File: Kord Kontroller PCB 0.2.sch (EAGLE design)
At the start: 190 parts, among them J1 MIDIOUTB, J2 MIDIOUTA, J3 FTSH-105-01-L-DV-KJ, SW2 SPST_TACT-KMR2, U1 AP2112K-3.3, U2 ATSAMD51J19A-AUT, U3 SN74LV4T125PWR, Y1 ECS-.327-12.5-17X-TR

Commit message: LED Variant and rewire
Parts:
- LED1, LED10, LED11, LED12, LED13, LED14, LED15, LED16, LED17, LED18, LED19, LED2, LED20, LED21, LED22, LED23, LED24, LED25, LED26, LED27, LED28, LED29, LED3, LED30, LED31, LED32, LED33, LED34, LED35, LED36, LED37, LED38, LED39, LED4, LED40, LED41, LED42, LED43, LED44, LED45, LED46, LED47, LED48, LED49, LED5, LED50, LED51, LED52, LED53, LED54, LED6, LED7, LED8, LED9: value WS2812B3535 -> WS2812BHRGB32M; device microbuilder:WS2812B3535 -> adafruit:WS2812BHRGB32M
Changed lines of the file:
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@@
 <part name="B10" library="microbuilder" deviceset="ELAST_10X10" device=""/>
 <part name="B14" library="microbuilder" deviceset="ELAST_10X10" device=""/>
-<part name="LED1" library="microbuilder" deviceset="WS2812B" device="3535"/>
-<part name="LED2" library="microbuilder" deviceset="WS2812B" device="3535"/>
-<part name="LED3" library="microbuilder" deviceset="WS2812B" device="3535"/>
-<part name="LED4" library="microbuilder" deviceset="WS2812B" device="3535"/>
-<part name="LED5" library="microbuilder" deviceset="WS2812B" device="3535"/>
-<part name="LED6" library="microbuilder" deviceset="WS2812B" device="3535"/>
-<part name="LED7" library="microbuilder" deviceset="WS2812B" device="3535"/>
-<part name="LED8" library="microbuilder" deviceset="WS2812B" device="3535"/>
-<part name="LED9" library="microbuilder" deviceset="WS2812B" device="3535"/>
-<part name="LED10" library="microbuilder" deviceset="WS2812B" device="3535"/>
-<part name="LED11" library="microbuilder" deviceset="WS2812B" device="3535"/>
-<part name="LED12" library="microbuilder" deviceset="WS2812B" device="3535"/>
-<part name="LED13" library="microbuilder" deviceset="WS2812B" device="3535"/>
-<part name="LED14" library="microbuilder" deviceset="WS2812B" device="3535"/>
-<part name="LED15" library="microbuilder" deviceset="WS2812B" device="3535"/>
-<part name="LED16" library="microbuilder" deviceset="WS2812B" device="3535"/>
+<part name="LED1" library="adafruit" deviceset="WS2812B" device="HRGB32M"/>
+<part name="LED2" library="adafruit" deviceset="WS2812B" device="HRGB32M"/>
+<part name="LED3" library="adafruit" deviceset="WS2812B" device="HRGB32M"/>
+<part name="LED4" library="adafruit" deviceset="WS2812B" device="HRGB32M"/>
+<part name="LED5" library="adafruit" deviceset="WS2812B" device="HRGB32M"/>
+<part name="LED6" library="adafruit" deviceset="WS2812B" device="HRGB32M"/>
+<part name="LED7" library="adafruit" deviceset="WS2812B" device="HRGB32M"/>
+<part name="LED8" library="adafruit" deviceset="WS2812B" device="HRGB32M"/>
+<part name="LED9" library="adafruit" deviceset="WS2812B" device="HRGB32M"/>
+<part name="LED10" library="adafruit" deviceset="WS2812B" device="HRGB32M"/>
+<part name="LED11" library="adafruit" deviceset="WS2812B" device="HRGB32M"/>
+<part name="LED12" library="adafruit" deviceset="WS2812B" device="HRGB32M"/>
+<part name="LED13" library="adafruit" deviceset="WS2812B" device="HRGB32M"/>
+<part name="LED14" library="adafruit" deviceset="WS2812B" device="HRGB32M"/>
+<part name="LED15" library="adafruit" deviceset="WS2812B" device="HRGB32M"/>
+<part name="LED16" library="adafruit" deviceset="WS2812B" device="HRGB32M"/>
 <part name="GND1" library="supply1" library_urn="urn:adsk.eagle:library:371" deviceset="GND" device=""/>
 <part name="GND8" library="supply1" library_urn="urn:adsk.eagle:library:371" deviceset="GND" device=""/>
-<part name="LED17" library="microbuilder" deviceset="WS2812B" device="3535"/>
-<part name="LED18" library="microbuilder" deviceset="WS2812B" device="3535"/>
-<part name="LED19" library="microbuilder" deviceset="WS2812B" device="3535"/>
-<part name="LED20" library="microbuilder" deviceset="WS2812B" device="3535"/>
-<part name="LED21" library="microbuilder" deviceset="WS2812B" device="3535"/>
-<part name="LED22" library="microbuilder" deviceset="WS2812B" device="3535"/>
-<part name="LED23" library="microbuilder" deviceset="WS2812B" device="3535"/>
-<part name="LED24" library="microbuilder" deviceset="WS2812B" device="3535"/>
-<part name="LED25" library="microbuilder" deviceset="WS2812B" device="3535"/>
-<part name="LED26" library="microbuilder" deviceset="WS2812B" device="3535"/>
-<part name="LED27" library="microbuilder" deviceset="WS2812B" device="3535"/>
-<part name="LED28" library="microbuilder" deviceset="WS2812B" device="3535"/>
-<part name="LED29" library="microbuilder" deviceset="WS2812B" device="3535"/>
-<part name="LED30" library="microbuilder" deviceset="WS2812B" device="3535"/>
-<part name="LED31" library="microbuilder" deviceset="WS2812B" device="3535"/>
-<part name="LED32" library="microbuilder" deviceset="WS2812B" device="3535"/>
+<part name="LED17" library="adafruit" deviceset="WS2812B" device="HRGB32M"/>
+<part name="LED18" library="adafruit" deviceset="WS2812B" device="HRGB32M"/>
+<part name="LED19" library="adafruit" deviceset="WS2812B" device="HRGB32M"/>
+<part name="LED20" library="adafruit" deviceset="WS2812B" device="HRGB32M"/>
+<part name="LED21" library="adafruit" deviceset="WS2812B" device="HRGB32M"/>
+<part name="LED22" library="adafruit" deviceset="WS2812B" device="HRGB32M"/>
+<part name="LED23" library="adafruit" deviceset="WS2812B" device="HRGB32M"/>
+<part name="LED24" library="adafruit" deviceset="WS2812B" device="HRGB32M"/>
+<part name="LED25" library="adafruit" deviceset="WS2812B" device="HRGB32M"/>
+<part name="LED26" library="adafruit" deviceset="WS2812B" device="HRGB32M"/>
+<part name="LED27" library="adafruit" deviceset="WS2812B" device="HRGB32M"/>
+<part name="LED28" library="adafruit" deviceset="WS2812B" device="HRGB32M"/>
+<part name="LED29" library="adafruit" deviceset="WS2812B" device="HRGB32M"/>
+<part name="LED30" library="adafruit" deviceset="WS2812B" device="HRGB32M"/>
+<part name="LED31" library="adafruit" deviceset="WS2812B" device="HRGB32M"/>
+<part name="LED32" library="adafruit" deviceset="WS2812B" device="HRGB32M"/>
 <part name="GND11" library="supply1" library_urn="urn:adsk.eagle:library:371" deviceset="GND" device=""/>
 <part name="GND12" library="supply1" library_urn="urn:adsk.eagle:library:371" deviceset="GND" device=""/>
@@
 <part name="U$13" library="microbuilder" deviceset="3.3V" device=""/>
 <part name="PTC1" library="microbuilder" deviceset="PTC" device="1206" value="500mA Fuse"/>
-<part name="LED33" library="microbuilder" deviceset="WS2812B" device="3535"/>
-<part name="LED34" library="microbuilder" deviceset="WS2812B" device="3535"/>
-<part name="LED35" library="microbuilder" deviceset="WS2812B" device="3535"/>
-<part name="LED36" library="microbuilder" deviceset="WS2812B" device="3535"/>
-<part name="LED37" library="microbuilder" deviceset="WS2812B" device="3535"/>
-<part name="LED38" library="microbuilder" deviceset="WS2812B" device="3535"/>
-<part name="LED39" library="microbuilder" deviceset="WS2812B" device="3535"/>
-<part name="LED40" library="microbuilder" deviceset="WS2812B" device="3535"/>
+<part name="LED33" library="adafruit" deviceset="WS2812B" device="HRGB32M"/>
+<part name="LED34" library="adafruit" deviceset="WS2812B" device="HRGB32M"/>
+<part name="LED35" library="adafruit" deviceset="WS2812B" device="HRGB32M"/>
+<part name="LED36" library="adafruit" deviceset="WS2812B" device="HRGB32M"/>
+<part name="LED37" library="adafruit" deviceset="WS2812B" device="HRGB32M"/>
+<part name="LED38" library="adafruit" deviceset="WS2812B" device="HRGB32M"/>
+<part name="LED39" library="adafruit" deviceset="WS2812B" device="HRGB32M"/>
+<part name="LED40" library="adafruit" deviceset="WS2812B" device="HRGB32M"/>
 <part name="GND10" library="supply1" library_urn="urn:adsk.eagle:library:371" deviceset="GND" device=""/>
-<part name="LED41" library="microbuilder" deviceset="WS2812B" device="3535"/>
-<part name="LED42" library="microbuilder" deviceset="WS2812B" device="3535"/>
-<part name="LED43" library="microbuilder" deviceset="WS2812B" device="3535"/>
-<part name="LED44" library="microbuilder" deviceset="WS2812B" device="3535"/>
-<part name="LED45" library="microbuilder" deviceset="WS2812B" device="3535"/>
-<part name="LED46" library="microbuilder" deviceset="WS2812B" device="3535"/>
-<part name="LED47" library="microbuilder" deviceset="WS2812B" device="3535"/>
-<part name="LED48" library="microbuilder" deviceset="WS2812B" device="3535"/>
+<part name="LED41" library="adafruit" deviceset="WS2812B" device="HRGB32M"/>
+<part name="LED42" library="adafruit" deviceset="WS2812B" device="HRGB32M"/>
+<part name="LED43" library="adafruit" deviceset="WS2812B" device="HRGB32M"/>
+<part name="LED44" library="adafruit" deviceset="WS2812B" device="HRGB32M"/>
+<part name="LED45" library="adafruit" deviceset="WS2812B" device="HRGB32M"/>
+<part name="LED46" library="adafruit" deviceset="WS2812B" device="HRGB32M"/>
+<part name="LED47" library="adafruit" deviceset="WS2812B" device="HRGB32M"/>
+<part name="LED48" library="adafruit" deviceset="WS2812B" device="HRGB32M"/>
 <part name="GND16" library="supply1" library_urn="urn:adsk.eagle:library:371" deviceset="GND" device=""/>
-<part name="LED49" library="microbuilder" deviceset="WS2812B" device="3535"/>
-<part name="LED50" library="microbuilder" deviceset="WS2812B" device="3535"/>
-<part name="LED51" library="microbuilder" deviceset="WS2812B" device="3535"/>
-<part name="LED52" library="microbuilder" deviceset="WS2812B" device="3535"/>
-<part name="LED53" library="microbuilder" deviceset="WS2812B" device="3535"/>
-<part name="LED54" library="microbuilder" deviceset="WS2812B" device="3535"/>
+<part name="LED49" library="adafruit" deviceset="WS2812B" device="HRGB32M"/>
+<part name="LED50" library="adafruit" deviceset="WS2812B" device="HRGB32M"/>
+<part name="LED51" library="adafruit" deviceset="WS2812B" device="HRGB32M"/>
+<part name="LED52" library="adafruit" deviceset="WS2812B" device="HRGB32M"/>
+<part name="LED53" library="adafruit" deviceset="WS2812B" device="HRGB32M"/>
+<part name="LED54" library="adafruit" deviceset="WS2812B" device="HRGB32M"/>
 <part name="GND17" library="supply1" library_urn="urn:adsk.eagle:library:371" deviceset="GND" device=""/>
 <part name="R3" library="SparkFun-Resistors" deviceset="220OHM-1/10W-1%(0603)" device="" value="220"/>

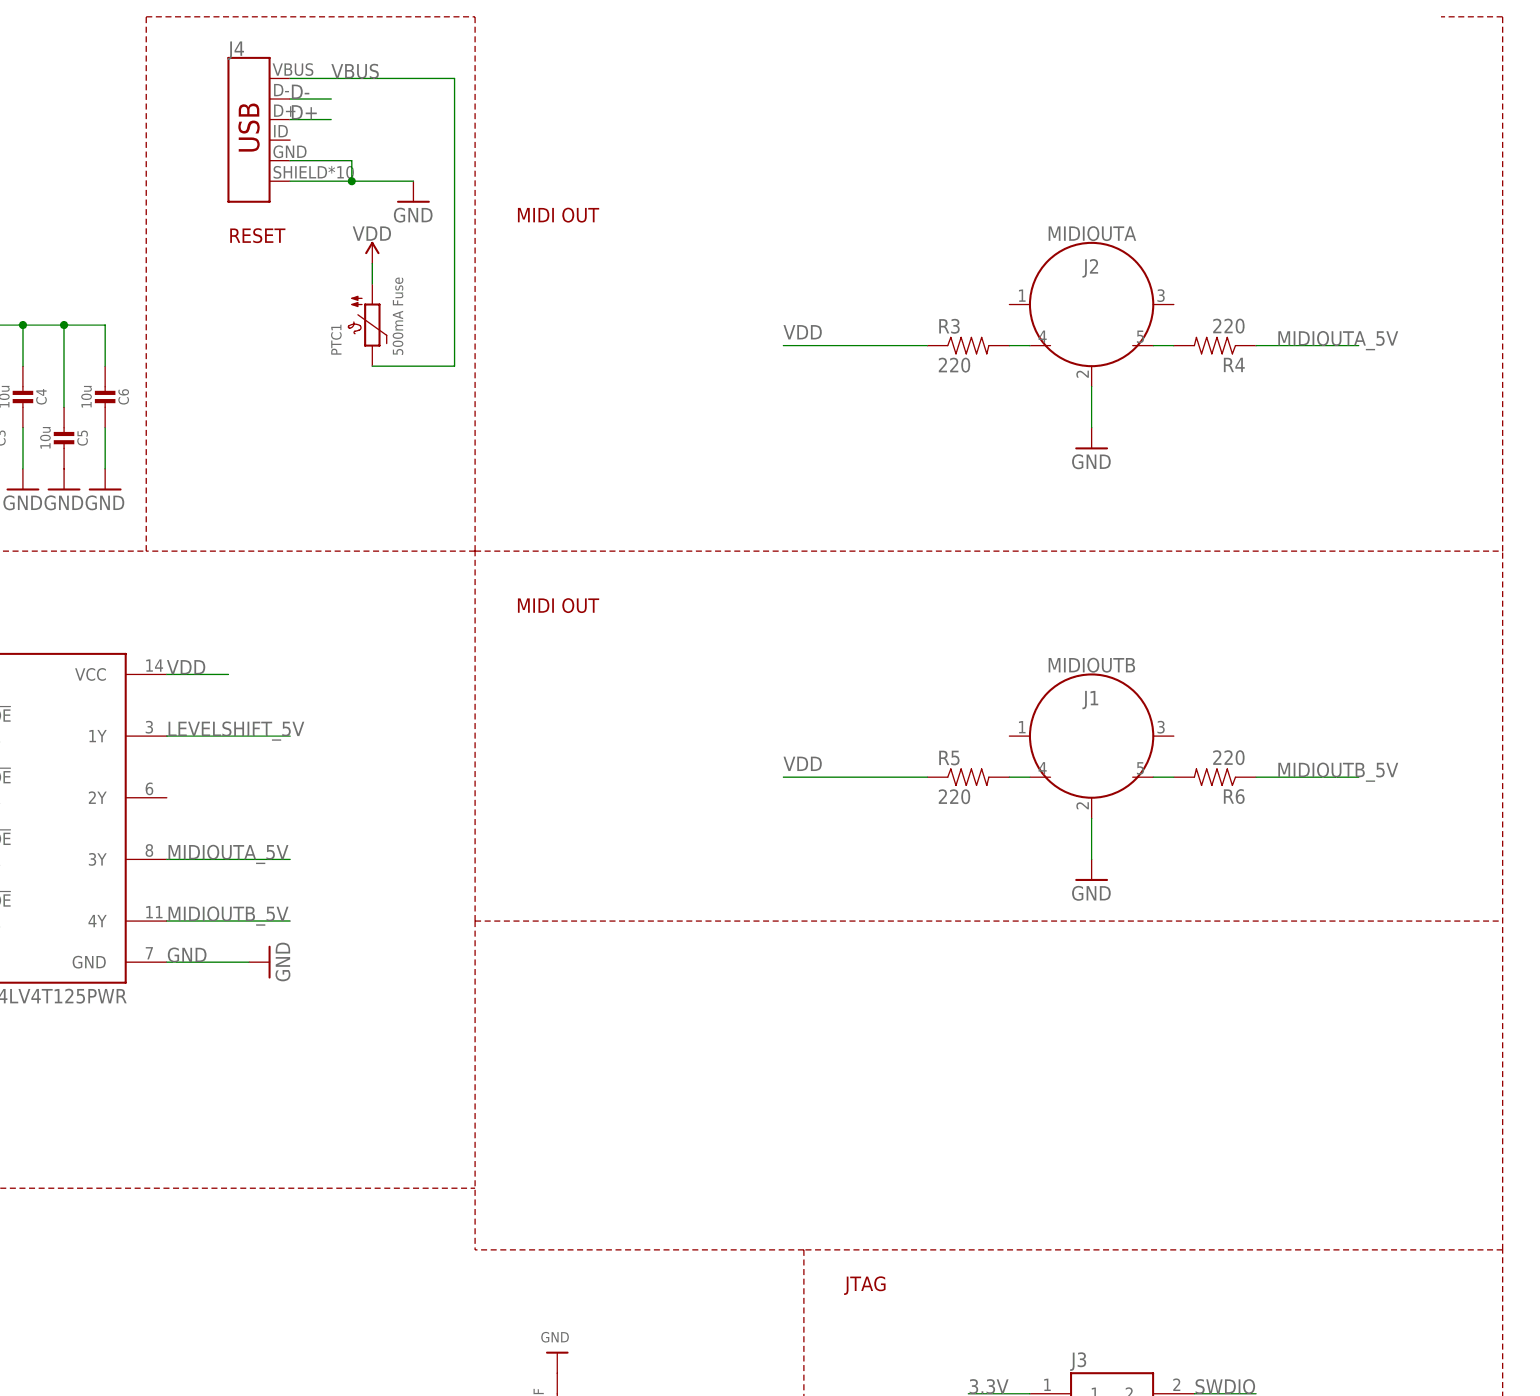
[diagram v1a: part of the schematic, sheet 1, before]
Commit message: added 2.5 mmtrs parts
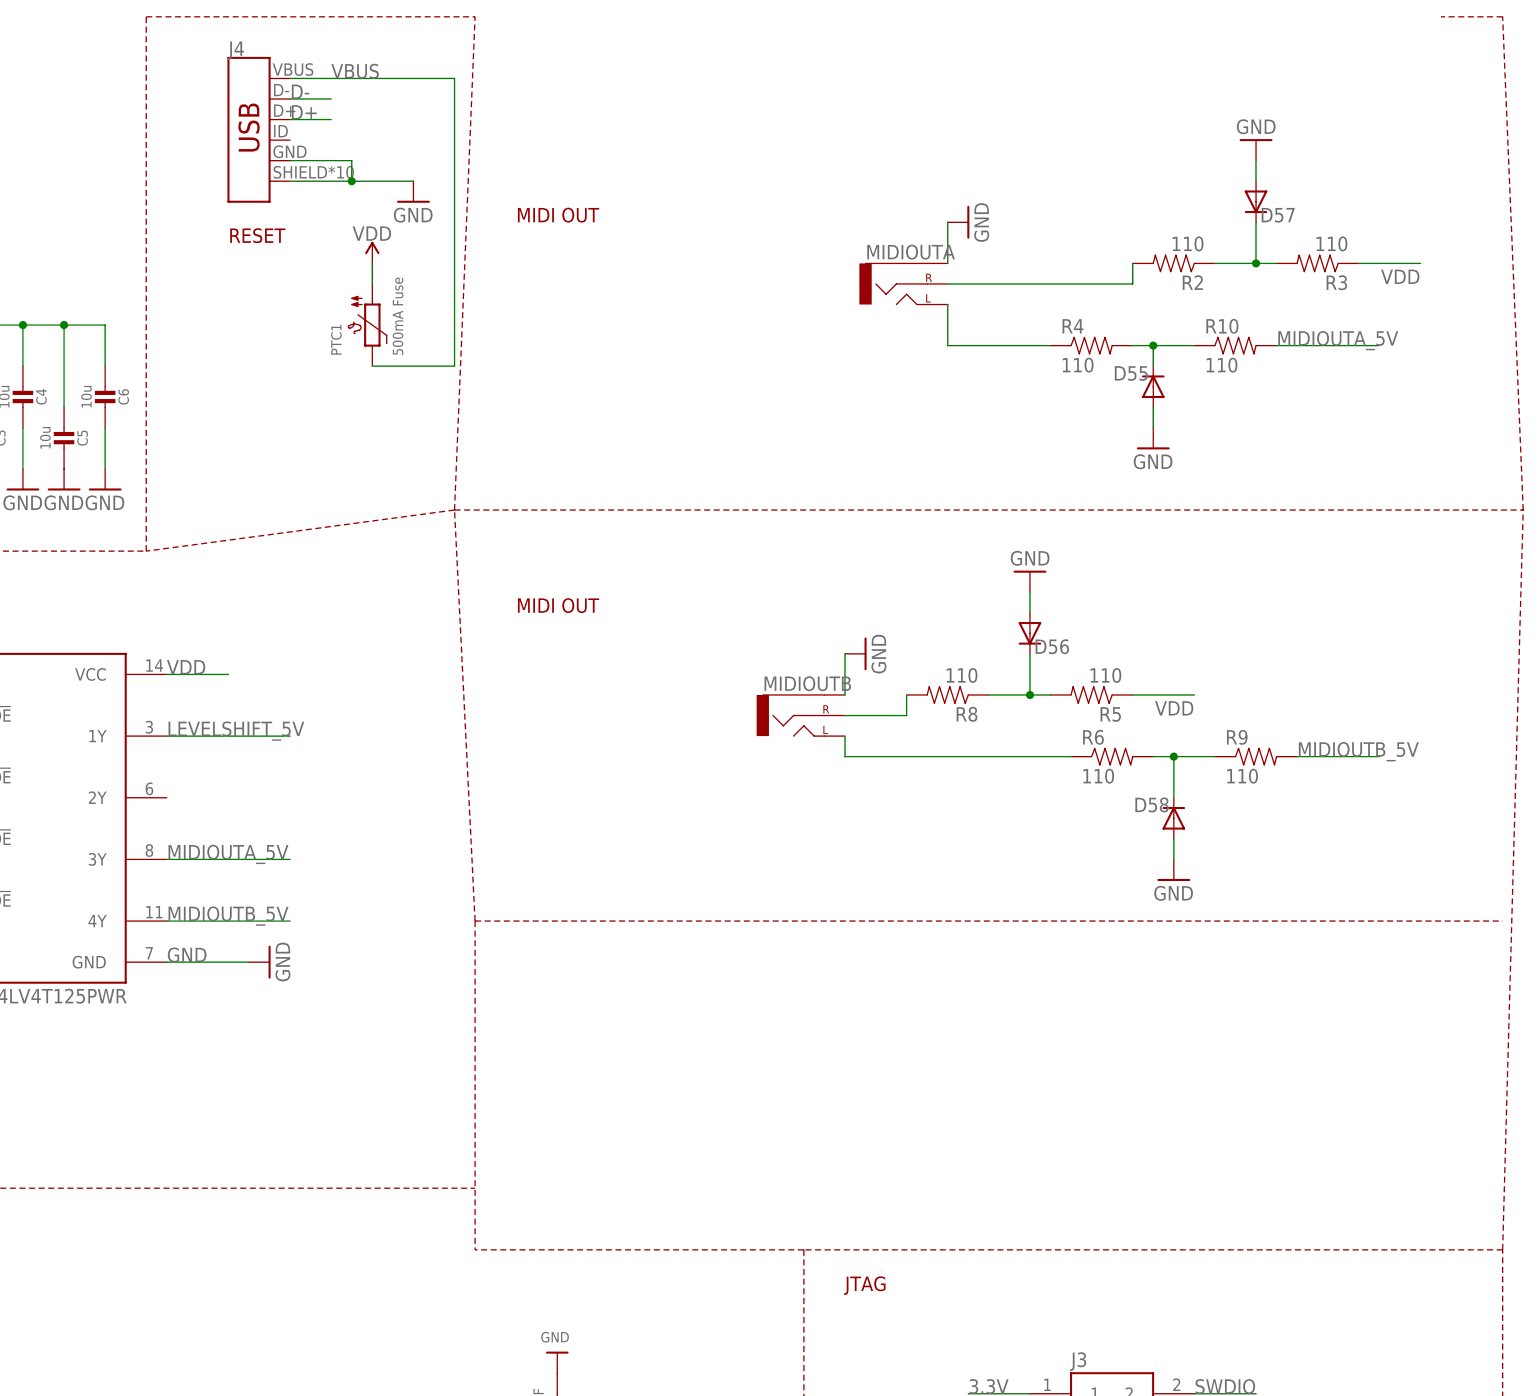
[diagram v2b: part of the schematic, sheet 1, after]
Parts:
- removed J1: MIDIOUTB, Testing:5-PIN-CIRCULAR-DINNEW
- removed J2: MIDIOUTA, Testing:5-PIN-CIRCULAR-DINNEW
- added D55, D56, D57, D58: (no value), diode:DIODE-SOD123
- added MIDIOUTA, MIDIOUTB: (no value), SparkFun-Connectors:AUDIO_JACK_2.5MM_2.5MM_SMD
- added R10, R2, R8, R9: 110, SparkFun-Resistors:220OHM-1/10W-1%(0603)
- R3, R4, R5, R6: value 220 -> 110
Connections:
- removed net N$114: J2.4, R3.2
- new net N$63: D57.C, R2.1, R3.2
- new net N$66: MIDIOUTA.RIGHT, R2.2
- new net N$69: D55.C, R10.1, R4.2
- new net N$71: D56.C, R5.2, R8.1
- new net N$72: MIDIOUTB.RIGHT, R8.2
- net GND: now also D55.A, D56.A, D57.A, D58.A, MIDIOUTA.SLEEVE, MIDIOUTB.SLEEVE; no longer J1.2, J2.2
- net MIDIOUTA_5V: now also R10.2; no longer R4.1
- net MIDIOUTB_5V: now also R9.2; no longer R6.1
- net N$1: now also MIDIOUTB.LEFT, R6.1; no longer J1.5, R6.2
- net N$110: now also MIDIOUTA.LEFT, R4.1; no longer J2.5, R4.2
- net N$2: now also D58.C, R6.2, R9.1; no longer J1.4, R5.2
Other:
- moved on the sheet: R3, R4, R5, R6
